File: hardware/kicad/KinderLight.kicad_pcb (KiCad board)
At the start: 2 copper layers, 63.5 x 30.5 mm, 16 parts, among them J2 VOUT, J3 ESP32C6 Left, J4 ESP32C6 Right, J5 VIN, J7 I2C BH1750, J8 LED, J9 +12VCC, Q1 AO3400A, Q2 AO3400A, Q3 AO3400A

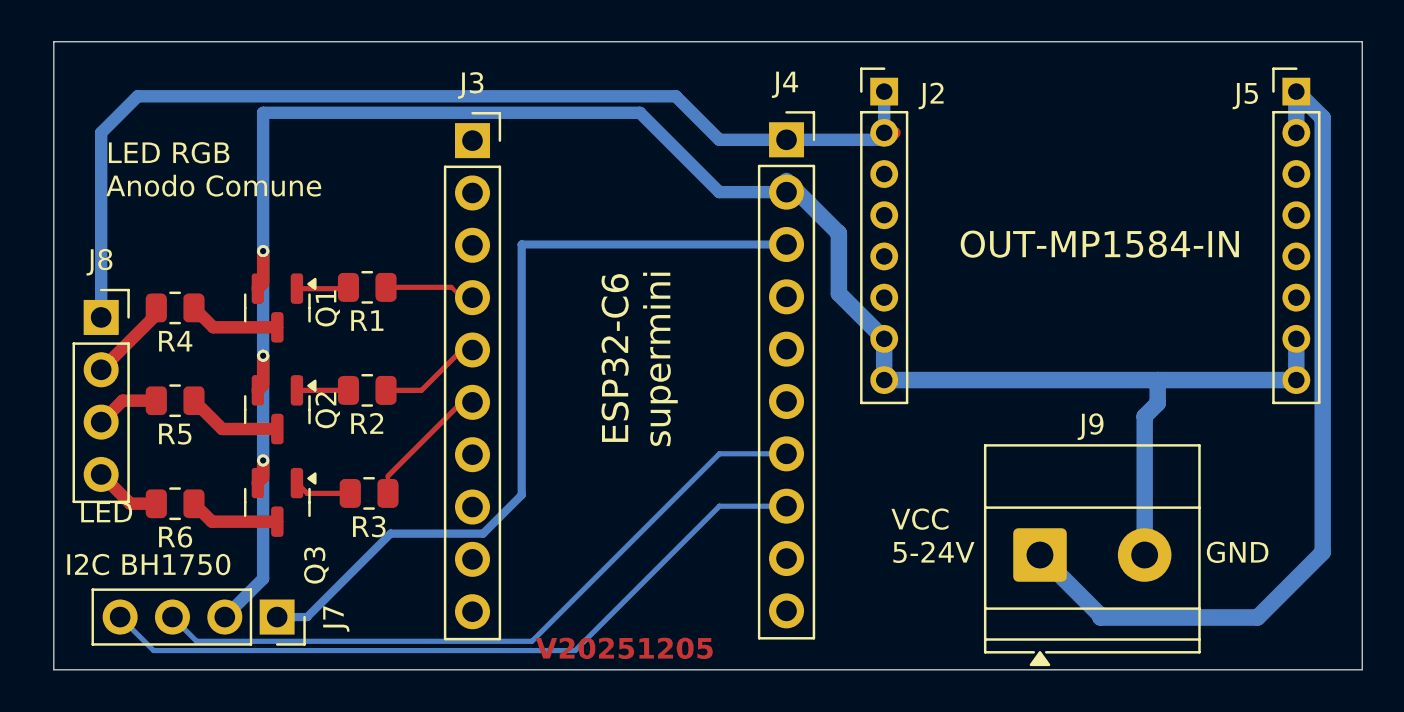
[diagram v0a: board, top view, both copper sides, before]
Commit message: Added version 20260207 of the PCB
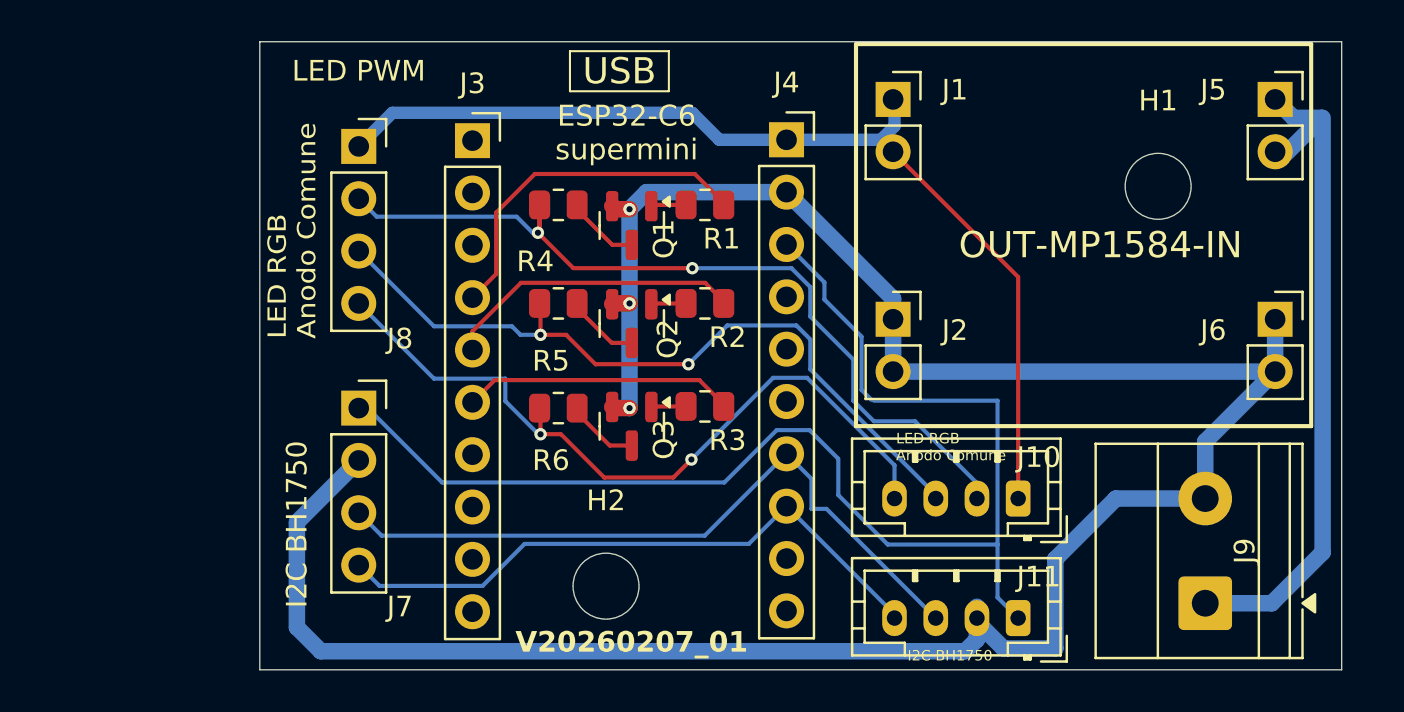
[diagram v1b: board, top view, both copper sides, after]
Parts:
- added H1: MountingHole, MountingHole:MountingHole_3.2mm_M3, F.Cu at (129.8, 75.6)
- added H2: MountingHole, MountingHole:MountingHole_3.2mm_M3, F.Cu at (103.0, 95.0)
- added J1: +5VCC, Connector_PinSocket_2.54mm:PinSocket_1x02_P2.54mm_Vertical, F.Cu at (116.9, 71.4)
- added J10: LED PWM JST, Connector_JST:JST_PH_B4B-PH-K_1x04_P2.00mm_Vertical, F.Cu at (123.0, 90.8)
- added J11: I2C BH1750 JST, Connector_JST:JST_PH_B4B-PH-K_1x04_P2.00mm_Vertical, F.Cu at (123.0, 96.5)
- added J6: GND, Connector_PinSocket_2.54mm:PinSocket_1x02_P2.54mm_Vertical, F.Cu at (135.5, 82.0)
- J2: value VOUT -> GND; footprint Connector_PinHeader_2.00mm:PinHeader_1x08_P2.00mm_Vertical -> Connector_PinSocket_2.54mm:PinSocket_1x02_P2.54mm_Vertical
- J5: value VIN -> VCC; footprint Connector_PinHeader_2.00mm:PinHeader_1x08_P2.00mm_Vertical -> Connector_PinSocket_2.54mm:PinSocket_1x02_P2.54mm_Vertical
- J8: value LED -> LED PWM
- moved R4 19.3 mm to (100.7, 76.5)
- moved R5 19.2 mm to (100.7, 81.3)
- moved R6 19.2 mm to (100.7, 86.4)
- moved Q2 17.7 mm to (104.2, 82.3)
- moved Q1 17.7 mm to (104.2, 77.5)
- moved Q3 17.6 mm to (104.2, 87.2)
- moved R2 16.9 mm to (107.8, 81.3)
- moved R1 16.9 mm to (107.8, 76.5)
- moved R3 16.8 mm to (107.8, 86.3)
- moved J8 15.0 mm to (91.0, 73.7)
- moved J2 11.1 mm to (116.9, 82.0)
- moved J7 10.9 mm to (91.0, 86.4), turned to 0 degrees
- moved J9 8.35 mm to (132.1, 95.8), turned to 90 degrees
- moved J5 1.10 mm to (135.5, 71.4)
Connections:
- net Net-(J4-Pin_3) renamed /3.3VDC
- net Net-(J8-Pin_2) renamed /LED RED
- net Net-(J8-Pin_3) renamed /LED GREEN
- net Net-(J8-Pin_4) renamed /LED BLUE
- J2 pad 1: VCC 5V -> GND
- J2 pad 2: VCC 5V -> GND
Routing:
- net /LED RED: track 4.11 -> 41.2 mm, vias 0 -> 2
- net /LED GREEN: track 3.11 -> 37.2 mm, vias 0 -> 2
- net /LED BLUE: track 3.26 -> 36.8 mm, vias 0 -> 2
- net /3.3VDC: track 39.3 -> 63.1 mm
- net GND: track 99.5 -> 122.3 mm
- net /PWM_RED: track 3.88 -> 17.1 mm
- net /PWM_GREEN: track 4.49 -> 14.6 mm
- net VCC 12V MAX: track 41.2 -> 32.9 mm
- net /PWM_BLUE: track 5.91 -> 13.3 mm
- net /I2C SDA: track 35.9 -> 30.7 mm
- net VCC 5V: track 51.2 -> 49.0 mm
- net Net-(Q3-G): track 2.79 -> 1.80 mm
- net Net-(Q2-D): track 4.62 -> 3.68 mm
- net Net-(Q3-D): track 4.41 -> 3.64 mm
- net Net-(Q1-D): track 4.44 -> 3.68 mm
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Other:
- board size 63.5 x 30.5 mm -> 52.5 x 30.5 mm
- board text added: "+3.3V"
- board text added: "+5V"
- board text added: "I2C BH1750"
- board text added: "USB"
- board text added: "V20260207_01"
- board text removed: "V20251205"

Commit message: Added the kicad source file of the production batch
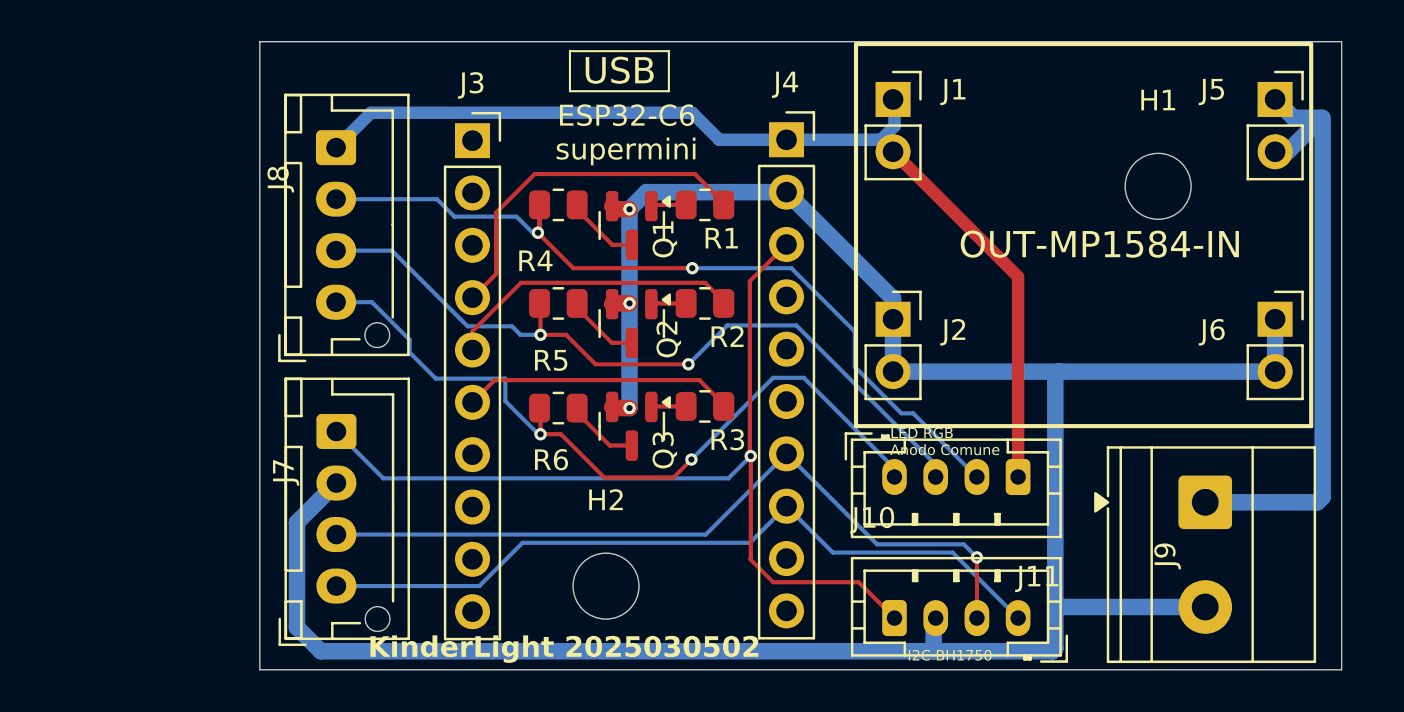
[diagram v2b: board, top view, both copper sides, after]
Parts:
- J7: value I2C BH1750 -> I2C BH1750 XH; footprint Connector_PinSocket_2.54mm:PinSocket_1x04_P2.54mm_Vertical -> Connector_JST:JST_XH_B4B-XH-AM_1x04_P2.50mm_Vertical
- J8: footprint Connector_PinSocket_2.54mm:PinSocket_1x04_P2.54mm_Vertical -> Connector_JST:JST_XH_B4B-XH-AM_1x04_P2.50mm_Vertical
- moved J7 8.70 mm to (89.9, 95.0), turned to 90 degrees
- moved J8 7.64 mm to (89.9, 81.2), turned to 90 degrees
- moved J10 6.09 mm to (117.0, 89.7), turned to 0 degrees
- moved J9 4.90 mm to (132.1, 90.9), turned to -90 degrees
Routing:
- net /3.3VDC: track 63.1 -> 45.8 mm, vias 0 -> 1
- net /I2C SDA: track 30.7 -> 37.3 mm
- net /I2C SCL: track 34.4 -> 38.2 mm, vias 0 -> 1
- net VCC 12V MAX: track 32.9 -> 29.3 mm
- net GND: track 122.3 -> 120.0 mm
- net VCC 5V: track 49.0 -> 49.9 mm
- net /LED BLUE: track 36.8 -> 37.7 mm
- net /LED RED: track 41.2 -> 40.4 mm
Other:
- board text added: "${TITLE} ${REVISION}"
- board text removed: "V20260207_01"
